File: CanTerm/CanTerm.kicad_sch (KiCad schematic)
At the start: 2 parts, among them J1 Conn_01x02

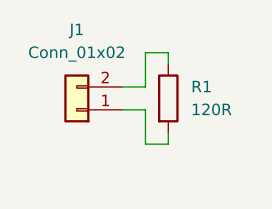
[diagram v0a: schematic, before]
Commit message: Added molexSL footprint and improved CanTerm
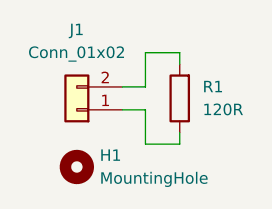
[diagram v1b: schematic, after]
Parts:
- added H1: MountingHole, MountingHole:MountingHole_5mm, symbol Mechanical:MountingHole
- J1: footprint Connector_PinHeader_2.54mm:PinHeader_1x02_P2.54mm_Horizontal -> FRC5010-FootprintLibrary:Molex_SL_RightAngle_Through_1x02
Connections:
- net at J1.1 (Pin_1): now also R1.1; no longer R1.2
- net at J1.2 (Pin_2): now also R1.2; no longer R1.1
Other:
- moved on the sheet: R1
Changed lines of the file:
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@@
 	(wire
 		(pts
-			(xy 91.44 86.36) (xy 93.98 86.36)
-		)
-		(stroke
-			(width 0)
-			(type default)
-		)
-	)
-	(wire
-		(pts
-			(xy 93.98 85.09) (xy 93.98 86.36)
+			(xy 91.44 86.36) (xy 95.25 86.36)
+		)
+		(stroke
+			(width 0)
+			(type default)
+		)
+	)
+	(wire
+		(pts
+			(xy 95.25 85.09) (xy 95.25 86.36)
 		)
 		(stroke
@@
 	(wire
 		(pts
-			(xy 91.44 76.2) (xy 93.98 76.2)
-		)
-		(stroke
-			(width 0)
-			(type default)
-		)
-	)
-	(wire
-		(pts
-			(xy 93.98 76.2) (xy 93.98 77.47)
+			(xy 91.44 76.2) (xy 95.25 76.2)
+		)
+		(stroke
+			(width 0)
+			(type default)
+		)
+	)
+	(wire
+		(pts
+			(xy 95.25 76.2) (xy 95.25 77.47)
 		)
 		(stroke
@@
 			)
 		)
-		(property "Footprint" "Connector_PinHeader_2.54mm:PinHeader_1x02_P2.54mm_Horizontal"
+		(property "Footprint" "FRC5010-FootprintLibrary:Molex_SL_RightAngle_Through_1x02"
 			(at 83.82 82.55 0)
 			(effects
@@
 	)
 	(symbol
+		(lib_id "Mechanical:MountingHole")
+		(at 83.82 88.9 0)
+		(unit 1)
+		(exclude_from_sim yes)
+		(in_bom no)
+		(on_board yes)
+		(dnp no)
+		(property "Reference" "H1"
+			(at 86.36 87.6299 0)
+			(effects
+				(font
+					(size 1.27 1.27)
+				)
+				(justify left)
+			)
+		)
+		(property "Value" "MountingHole"
+			(at 86.36 90.1699 0)
+			(effects
+				(font
+					(size 1.27 1.27)
+				)
+				(justify left)
+			)
+		)
+		(property "Footprint" "MountingHole:MountingHole_5mm"
+			(at 83.82 88.9 0)
+			(effects
+				(font
+					(size 1.27 1.27)
+				)
+				(hide yes)
+			)
+		)
+		(property "Datasheet" "~"
+			(at 83.82 88.9 0)
+			(effects
+				(font
+					(size 1.27 1.27)
+				)
+				(hide yes)
+			)
+		)
+		(property "Description" "Mounting Hole without connection"
+			(at 83.82 88.9 0)
+			(effects
+				(font
+					(size 1.27 1.27)
+				)
+				(hide yes)
+			)
+		)
+		(instances
+			(project "CanTerm"
+				(path "/cdd6529d-9484-4876-b4bb-c46d8fc72074"
+					(reference "H1")
+					(unit 1)
+				)
+			)
+		)
+	)
+	(symbol
 		(lib_id "Device:R")
-		(at 93.98 81.28 0)
+		(at 95.25 81.28 180)
 		(unit 1)
 		(exclude_from_sim no)
@@
 		(fields_autoplaced yes)
 		(property "Reference" "R1"
-			(at 96.52 80.0099 0)
-			(effects
-				(font
-					(size 1.27 1.27)
-				)
-				(justify left)
+			(at 97.79 80.0099 0)
+			(effects
+				(font
+					(size 1.27 1.27)
+				)
+				(justify right)
 			)
 		)
 		(property "Value" "120R"
-			(at 96.52 82.5499 0)
-			(effects
-				(font
-					(size 1.27 1.27)
-				)
-				(justify left)
+			(at 97.79 82.5499 0)
+			(effects
+				(font
+					(size 1.27 1.27)
+				)
+				(justify right)
 			)
 		)
 		(property "Footprint" "Resistor_SMD:R_1206_3216Metric_Pad1.30x1.75mm_HandSolder"
-			(at 92.202 81.28 90)
+			(at 97.028 81.28 90)
 			(effects
 				(font
@@
 		)
 		(property "Datasheet" "~"
-			(at 93.98 81.28 0)
+			(at 95.25 81.28 0)
 			(effects
 				(font
@@
 		)
 		(property "Description" "Resistor"
-			(at 93.98 81.28 0)
-			(effects
-				(font
+			(at 95.25 81.28 0)
+			(effects
+				(font
